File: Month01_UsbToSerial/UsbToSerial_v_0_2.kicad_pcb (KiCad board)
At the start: 2 copper layers, 34.9 x 20.3 mm, 14 parts, among them J1 USB_B_Micro, J2 Conn_01x07_Female, J3 Conn_01x07_Female, U1 FT232RL

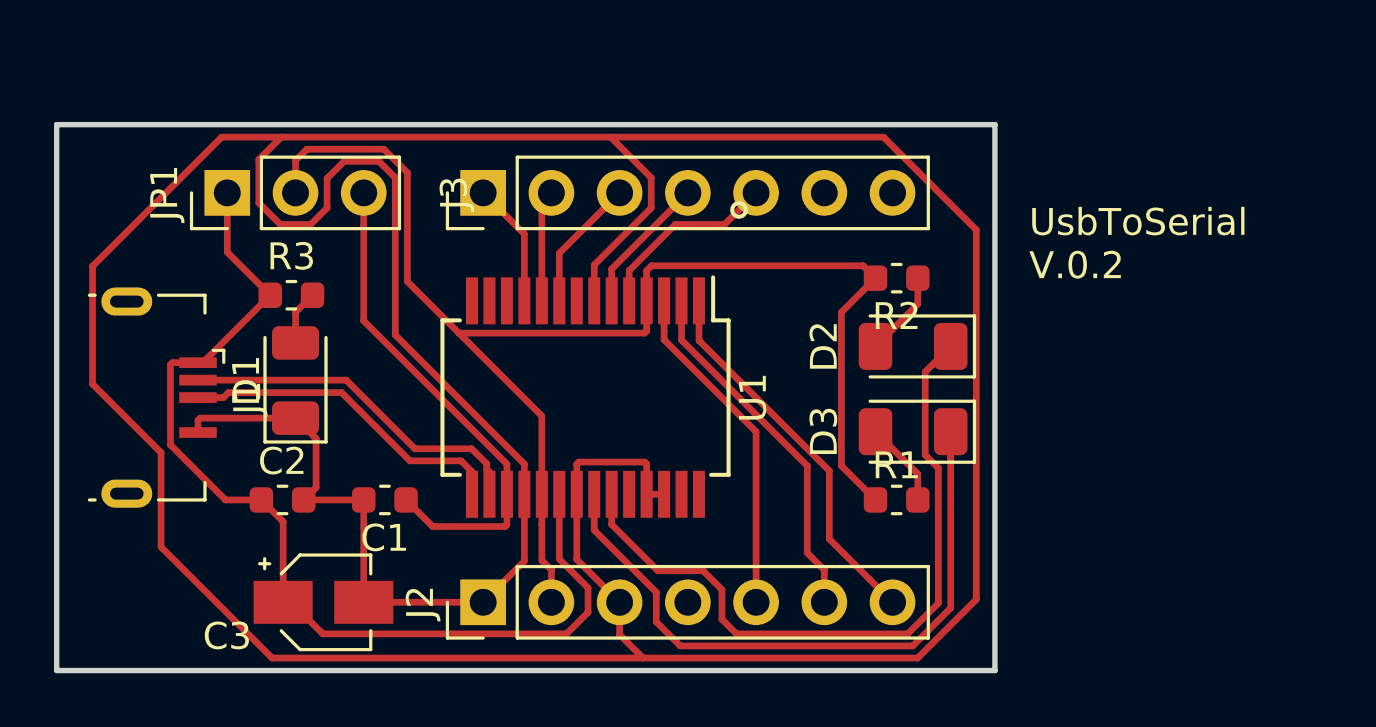
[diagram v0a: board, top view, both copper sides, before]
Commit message: Added new layout with reduced footprint
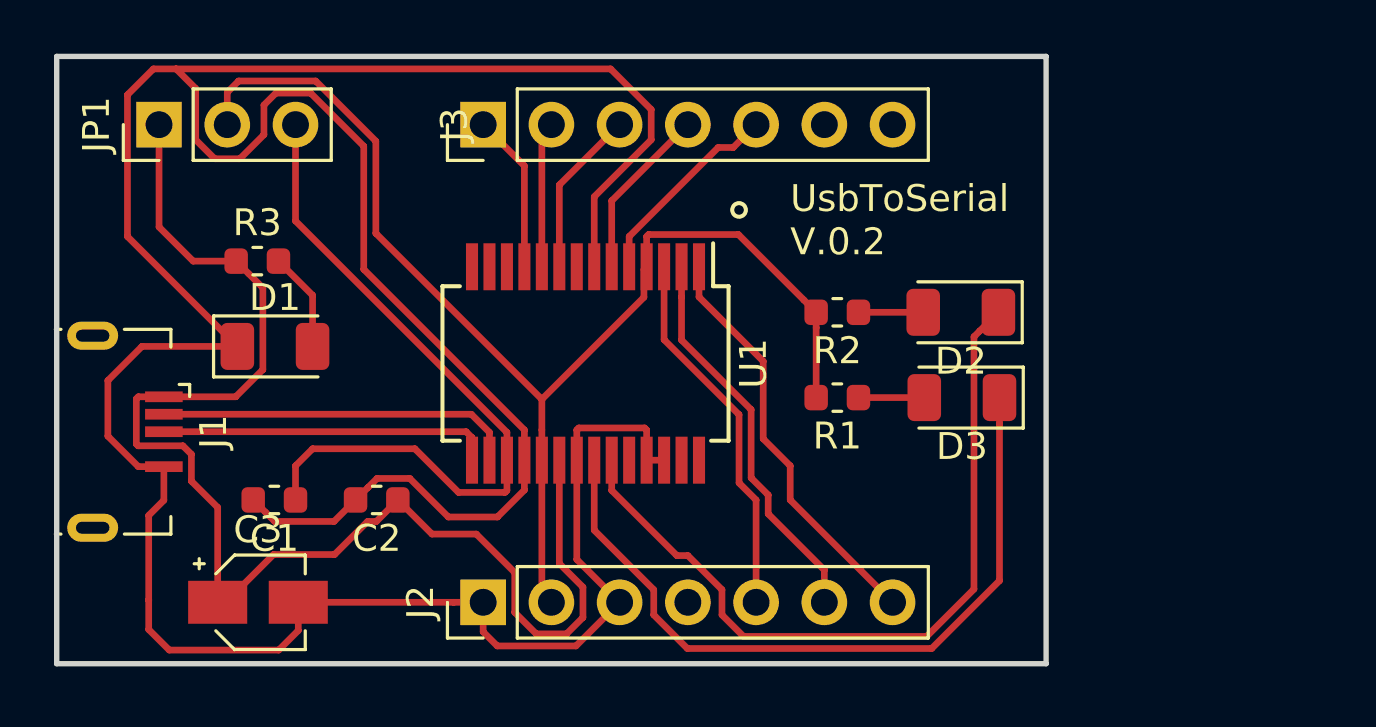
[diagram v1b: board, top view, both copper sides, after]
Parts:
- moved R1 4.40 mm to (105.9, 80.0)
- moved C1 4.11 mm to (84.9, 83.8)
- moved JP1 3.59 mm to (80.6, 69.8)
- moved C2 3.50 mm to (88.7, 83.8), turned to 180 degrees
- moved R2 2.55 mm to (105.9, 76.8)
- moved J3 2.54 mm to (92.7, 69.8)
- moved C3 2.44 mm to (84.3, 87.6)
- moved D3 2.22 mm to (110.5, 80.0)
- moved D2 2.18 mm to (110.5, 76.8)
- moved R3 1.80 mm to (84.3, 74.9)
- moved J1 1.80 mm to (79.4, 81.3)
- moved D1 1.48 mm to (85.0, 78.1), turned to 0 degrees
- moved U1 1.27 mm to (96.5, 78.7)
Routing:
- net GNDREF: track 161.5 -> 126.6 mm
- net +5V: track 37.6 -> 51.2 mm
- net +3V3: track 18.7 -> 27.0 mm
- net PWR: track 51.5 -> 46.1 mm
- net Net-(D3-Pad1): track 24.2 -> 27.9 mm
- net Net-(D2-Pad1): track 26.2 -> 28.8 mm
- net Net-(D1-Pad2): track 2.04 -> 3.70 mm
- net DCR: track 4.95 -> 6.22 mm
- net DCD: track 4.17 -> 5.44 mm
- net RI: track 5.19 -> 6.46 mm
- net CTS: track 4.66 -> 5.93 mm
- net RTS: track 12.6 -> 13.9 mm
- net TX0: track 14.2 -> 15.5 mm
- net DTR: track 13.4 -> 14.7 mm
- net Net-(D2-Pad2): track 3.19 -> 2.41 mm
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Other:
- board size 34.9 x 20.3 mm -> 36.8 x 22.6 mm
